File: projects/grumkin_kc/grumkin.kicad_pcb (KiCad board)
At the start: 2 copper layers, 26 parts, among them Q1 MOS_N, Q2 MOS_N, Q3 MOS_N, Q4 MOS_N, Q5 MOS_N, Q6 MOS_N

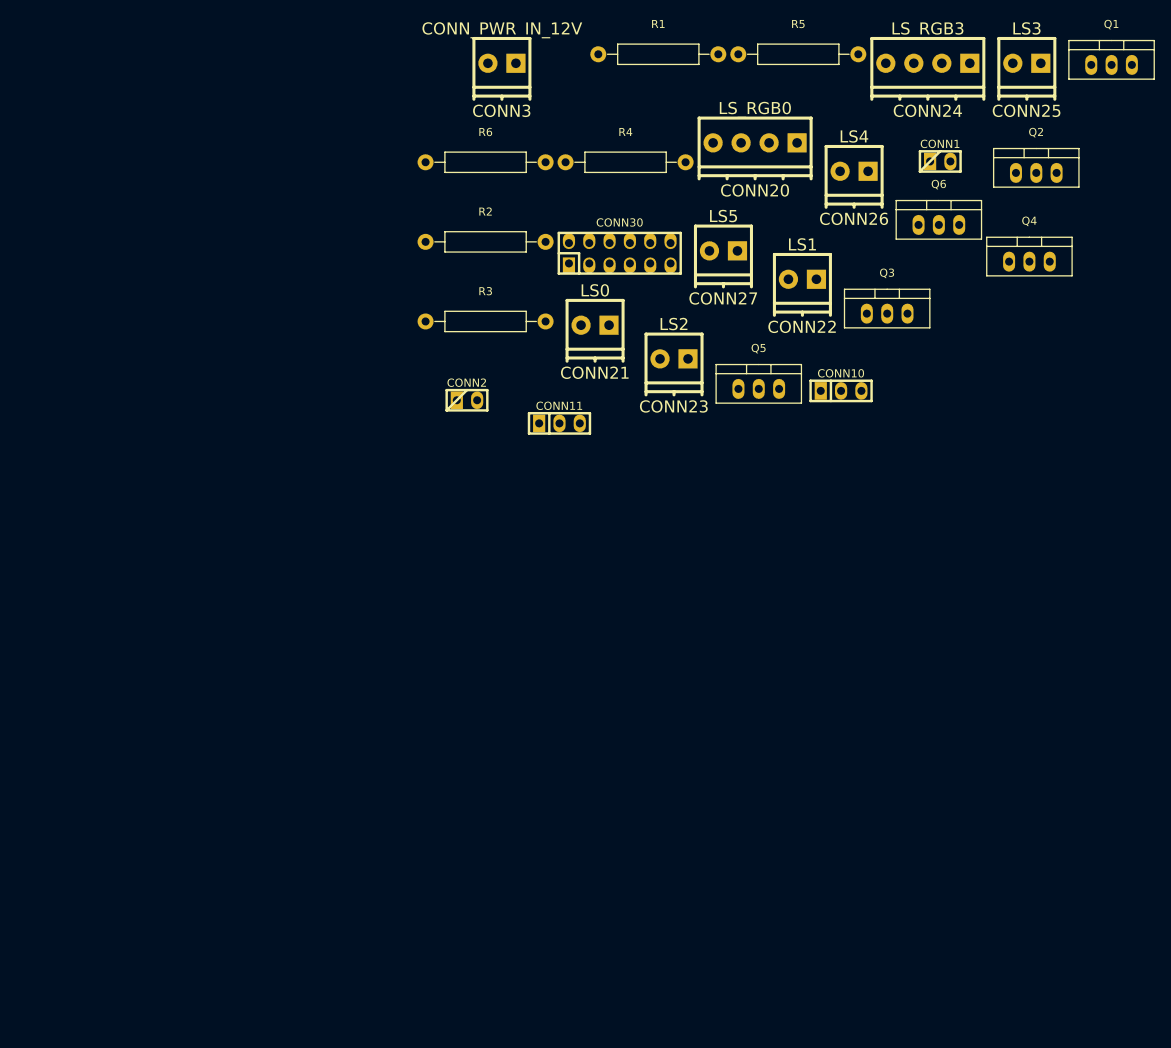
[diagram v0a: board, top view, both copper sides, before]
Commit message: PCB: Arranging footprints
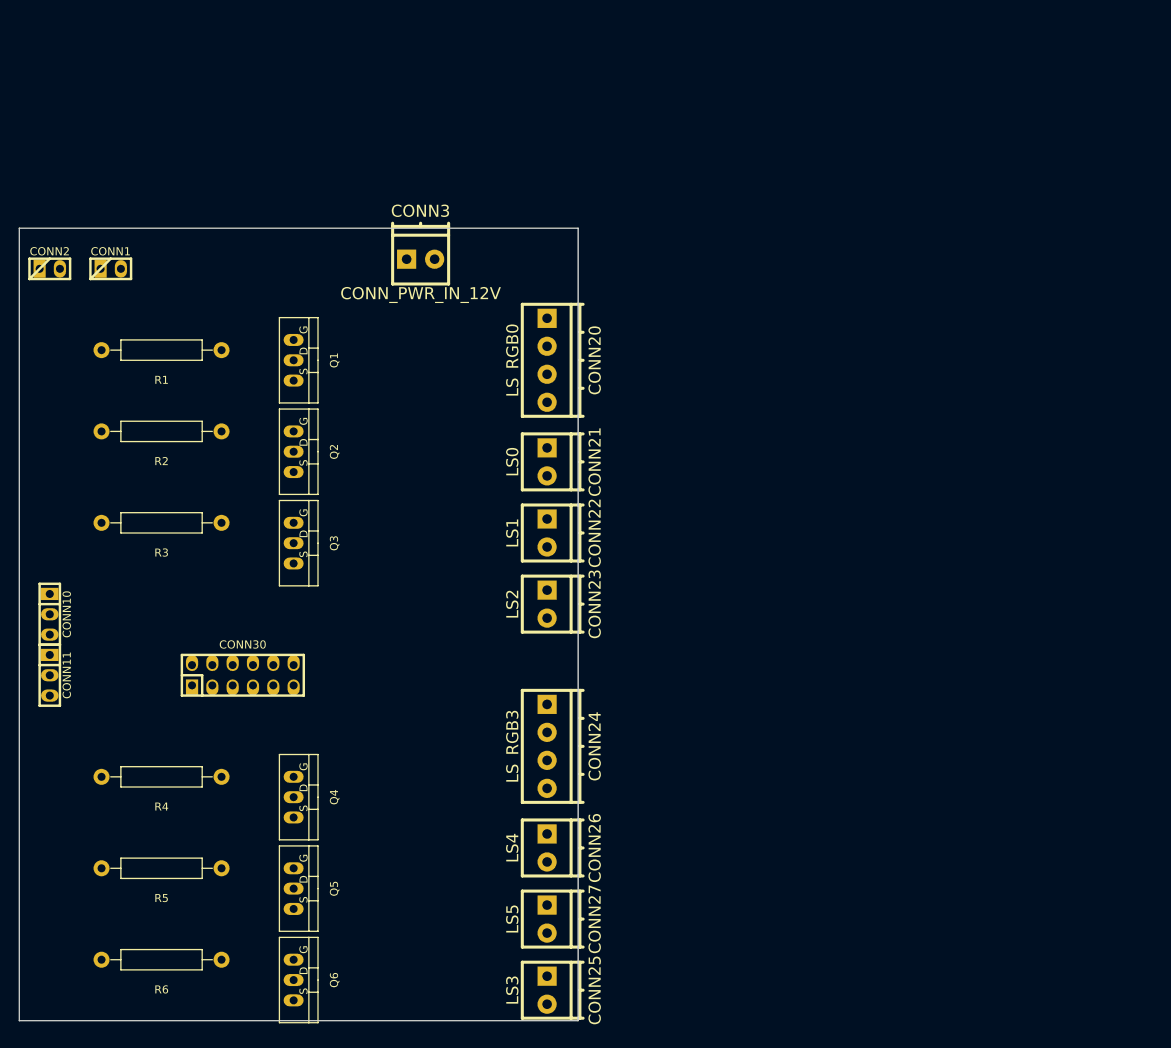
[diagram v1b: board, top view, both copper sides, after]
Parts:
- Q1, Q2, Q3, Q4, Q5, Q6: footprint Transistors_TO-220:TO-220_Neutral123_Vertical -> Transistors_TO-220:TO-220_FET-GDS_Vertical
- moved CONN25 129.5 mm to (116.2, 152.4), turned to 90 degrees
- moved R5 129.2 mm to (67.3, 137.2), turned to 180 degrees
- moved Q6 124.2 mm to (83.8, 151.1), turned to 270 degrees
- moved Q4 113.8 mm to (83.8, 128.3), turned to 270 degrees
- moved Q1 108.7 mm to (83.8, 73.7), turned to 270 degrees
- moved R6 107.6 mm to (67.3, 148.6), turned to 180 degrees
- moved CONN1 104.6 mm to (61.0, 62.2)
- moved CONN10 102.8 mm to (53.3, 105.4), turned to 270 degrees
- moved Q2 99.2 mm to (83.8, 85.1), turned to 270 degrees
- moved CONN24 96.8 mm to (116.2, 121.9), turned to 90 degrees
- moved R4 96.3 mm to (67.3, 125.7), turned to 180 degrees
- moved CONN26 92.0 mm to (116.2, 134.6), turned to 90 degrees
- moved CONN27 85.5 mm to (116.2, 143.5), turned to 90 degrees
- moved Q5 85.3 mm to (83.8, 139.7), turned to 270 degrees
- moved Q3 79.5 mm to (83.8, 96.5), turned to 270 degrees
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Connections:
- CONN20 pad 2: Net-(CONN20-Pad2) -> /LED_POWER
- CONN20 pad 3: Net-(CONN20-Pad3) -> /LED_POWER
- CONN20 pad 4: Net-(CONN20-Pad4) -> /LED_POWER
- CONN21 pad 2: Net-(CONN20-Pad2) -> /LED_POWER
- CONN22 pad 2: Net-(CONN20-Pad3) -> /LED_POWER
- CONN23 pad 2: Net-(CONN20-Pad4) -> /LED_POWER
- CONN24 pad 2: Net-(CONN24-Pad2) -> /LED_POWER
- CONN24 pad 3: Net-(CONN24-Pad3) -> /LED_POWER
- CONN24 pad 4: Net-(CONN24-Pad4) -> /LED_POWER
- CONN25 pad 2: Net-(CONN24-Pad2) -> /LED_POWER
- CONN26 pad 2: Net-(CONN24-Pad3) -> /LED_POWER
- CONN27 pad 2: Net-(CONN24-Pad4) -> /LED_POWER
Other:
- board outline added: 69.8 x 99.1 mm
- net class LED Power added: clearance 0.4, trace_width 1.5, via_dia 1, via_drill 0.8
- net class Power added: clearance 0.254, trace_width 0.254, via_dia 0.889, via_drill 0.635

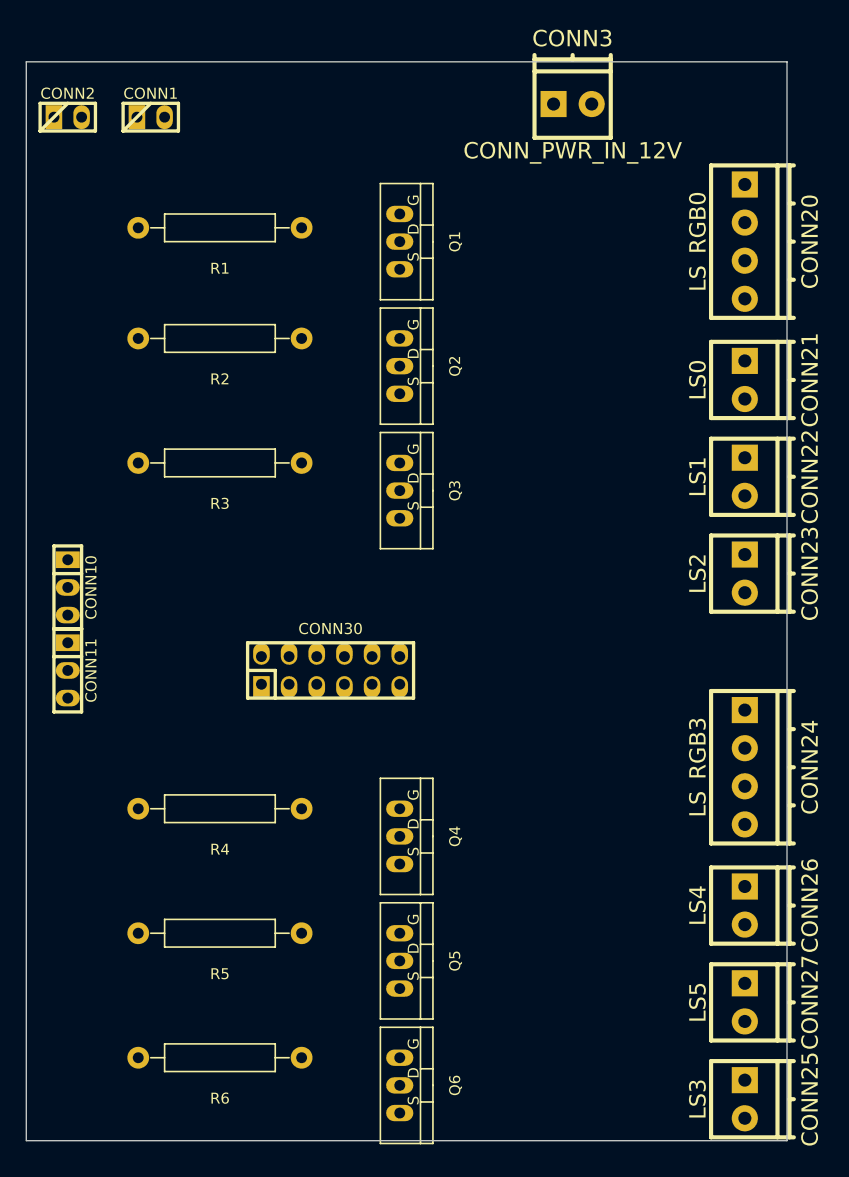
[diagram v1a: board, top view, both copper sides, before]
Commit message: Adding wires and texts to PCB
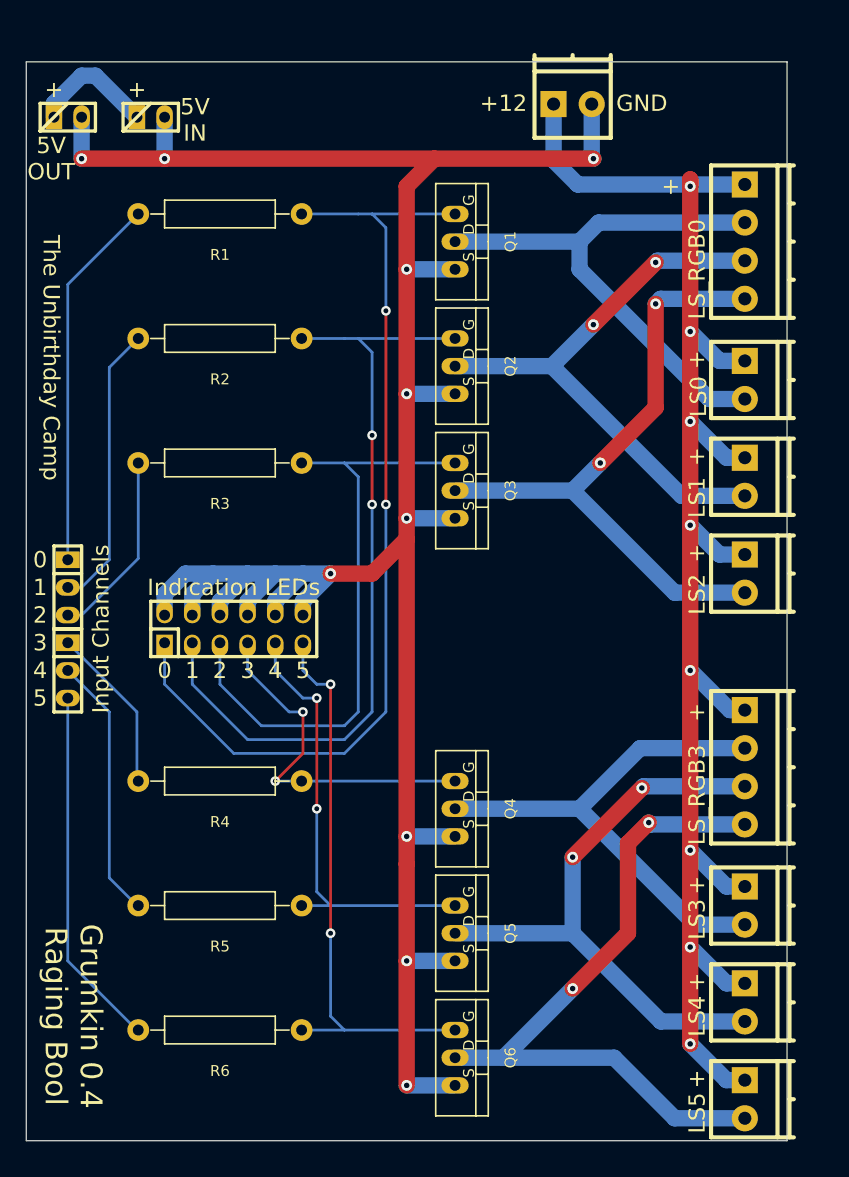
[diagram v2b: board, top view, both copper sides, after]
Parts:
- moved CONN25 17.8 mm to (116.2, 134.6)
- moved CONN30 9.67 mm to (68.6, 109.2)
- moved CONN27 8.89 mm to (116.2, 152.4)
- moved CONN26 8.89 mm to (116.2, 143.5)
- moved Q4 5.68 mm to (88.9, 125.7)
- moved Q5 5.68 mm to (88.9, 137.2)
- moved Q6 5.68 mm to (88.9, 148.6)
- moved Q1 5.08 mm to (88.9, 73.7)
- moved Q2 5.08 mm to (88.9, 85.1)
- moved Q3 5.08 mm to (88.9, 96.5)
- moved R4 2.54 mm to (67.3, 123.2)
- moved R5 2.54 mm to (67.3, 134.6)
- moved R6 2.54 mm to (67.3, 146.1)
- moved R1 1.27 mm to (67.3, 71.1)
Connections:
- CONN20 pad 2: /LED_POWER -> /LED_POWER_CH0
- CONN20 pad 3: /LED_POWER -> /LED_POWER_CH1
- CONN20 pad 4: /LED_POWER -> /LED_POWER_CH2
- CONN21 pad 2: /LED_POWER -> /LED_POWER_CH0
- CONN22 pad 2: /LED_POWER -> /LED_POWER_CH1
- CONN23 pad 2: /LED_POWER -> /LED_POWER_CH2
- CONN24 pad 2: /LED_POWER -> /LED_POWER_CH3
- CONN24 pad 3: /LED_POWER -> /LED_POWER_CH4
- CONN24 pad 4: /LED_POWER -> /LED_POWER_CH5
- CONN25 pad 2: /LED_POWER -> /LED_POWER_CH3
- CONN26 pad 2: /LED_POWER -> /LED_POWER_CH4
- CONN27 pad 2: /LED_POWER -> /LED_POWER_CH5
- CONN30 pad 11: GND -> Net-(CONN30-Pad11)
- CONN30 pad 2: Net-(CONN30-Pad2) -> GND
- CONN30 pad 4: Net-(CONN30-Pad4) -> GND
- CONN30 pad 6: Net-(CONN30-Pad6) -> GND
- CONN30 pad 7: GND -> Net-(CONN30-Pad7)
- CONN30 pad 9: GND -> Net-(CONN30-Pad9)
- Q1 pad D: /LED_POWER -> /LED_POWER_CH0
- Q2 pad D: /LED_POWER -> /LED_POWER_CH1
- Q2 pad G: Net-(CONN30-Pad2) -> Net-(CONN30-Pad3)
- Q3 pad D: /LED_POWER -> /LED_POWER_CH2
- Q3 pad G: Net-(CONN30-Pad3) -> Net-(CONN30-Pad5)
- Q4 pad D: /LED_POWER -> /LED_POWER_CH3
- Q4 pad G: Net-(CONN30-Pad4) -> Net-(CONN30-Pad7)
- Q5 pad D: /LED_POWER -> /LED_POWER_CH4
- Q5 pad G: Net-(CONN30-Pad5) -> Net-(CONN30-Pad9)
- Q6 pad D: /LED_POWER -> /LED_POWER_CH5
- Q6 pad G: Net-(CONN30-Pad6) -> Net-(CONN30-Pad11)
- R2 pad 1: Net-(CONN30-Pad2) -> Net-(CONN30-Pad3)
- R3 pad 1: Net-(CONN30-Pad3) -> Net-(CONN30-Pad5)
- R4 pad 1: Net-(CONN30-Pad4) -> Net-(CONN30-Pad7)
- R5 pad 1: Net-(CONN30-Pad5) -> Net-(CONN30-Pad9)
- R6 pad 1: Net-(CONN30-Pad6) -> Net-(CONN30-Pad11)
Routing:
- net GND: track 0.00 -> 222.8 mm, vias 0 -> 10
- net +12V: track 0.00 -> 148.5 mm, vias 0 -> 8
- net Net-(CONN30-Pad1): track 0.00 -> 88.8 mm, vias 0 -> 2
- net Net-(CONN30-Pad3): track 0.00 -> 72.5 mm, vias 0 -> 2
- net /LED_POWER_CH5: track 0.00 -> 64.9 mm, vias 0 -> 2
- net /LED_POWER_CH2: track 0.00 -> 59.2 mm, vias 0 -> 2
- net Net-(CONN30-Pad5): track 0.00 -> 56.2 mm
- net /LED_POWER_CH4: track 0.00 -> 55.4 mm, vias 0 -> 2
- net /LED_POWER_CH1: track 0.00 -> 53.3 mm, vias 0 -> 2
- net Net-(CONN30-Pad11): track 0.00 -> 52.0 mm, vias 0 -> 2
- net /LED_POWER_CH0: track 0.00 -> 50.0 mm
- net /LED_POWER_CH3: track 0.00 -> 48.5 mm
- net Net-(CONN30-Pad9): track 0.00 -> 41.1 mm, vias 0 -> 2
- net Net-(CONN10-Pad1): track 0.00 -> 34.4 mm
- net Net-(CONN11-Pad3): track 0.00 -> 33.2 mm
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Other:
- net class Power: clearance 0.254 -> 0.4; trace_width 0.254 -> 1.5; via_dia 0.889 -> 1; via_drill 0.635 -> 0.8
- board text added: "+"
- board text added: "+12"
- board text added: "0"
- board text added: "1"
- board text added: "2"
- board text added: "3"
- board text added: "4"
- board text added: "5"
- board text added: "5V IN"
- board text added: "5V OUT"
- board text added: "GND"
- board text added: "Grumkin 0.4 Raging Bool"
- board text added: "Indication LEDs"
- board text added: "Input Channels"
- board text added: "The Unbirthday Camp"

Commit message: PCB: Improving labels
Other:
- board text added: "B"
- board text added: "G"
- board text added: "R"

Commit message: Version: 0.4.0.0=>0.5.0.0
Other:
- board text added: "Grumkin 0.5 Raging Bool"
- board text removed: "Grumkin 0.4 Raging Bool"
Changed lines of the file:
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@@
   (title_block
     (title Grumkin)
-    (rev 0.4)
+    (rev 0.5)
     (company "Raging Bool")
     (comment 1 "Grumkin: A 6-channel PWM LED driver")
@@
     (effects (font (size 1.5 1.5) (thickness 0.3)))
   )
-  (gr_text "Grumkin 0.4\nRaging Bool" (at 53.848 144.78 270) (layer F.SilkS)
+  (gr_text "Grumkin 0.5\nRaging Bool" (at 53.848 144.78 270) (layer F.SilkS)
     (effects (font (size 2 2) (thickness 0.4)))
   )
